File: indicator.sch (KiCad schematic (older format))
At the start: 5 parts, among them U420 2N7002DW

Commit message: added test points
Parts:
- added J? (x2): TEST_1P, SFUSat:Measurement_Point_Round-SMD-Pad_Big, symbol TEST_1P
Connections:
- wire segments 10 -> 11
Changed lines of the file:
@@
 Connection ~ 6425 3025
 Wire Wire Line
-	6125 3025 6425 3025
-Wire Wire Line
-	6425 3025 6725 3025
+	6125 3025 6725 3025
 Wire Wire Line
 	4975 3775 5075 3775
@@
 Text HLabel 6725 3025 2    54   Input ~ 0
 3V3
+$Comp
+L TEST_1P J?
+U 1 1 5AD72D99
+P 5025 3700
+AR Path="/5AC903D9/5AD72D99" Ref="J?"  Part="1"
+AR Path="/5AC9A534/5AD72D99" Ref="J?"  Part="1"
+F 0 "J?" H 5025 3970 50  0000 C CNN
+F 1 "TEST_1P" H 5025 3900 50  0000 C CNN
+F 2 "SFUSat:Measurement_Point_Round-SMD-Pad_Big" H 5225 3700 50  0001 C CNN
+F 3 "" H 5225 3700 50  0001 C CNN
+	1    5025 3700
+	1    0    0    -1
+$EndComp
+$Comp
+L TEST_1P J?
+U 1 1 5AD72E22
+P 5025 4050
+AR Path="/5AC903D9/5AD72E22" Ref="J?"  Part="1"
+AR Path="/5AC9A534/5AD72E22" Ref="J?"  Part="1"
+F 0 "J?" H 5025 4320 50  0000 C CNN
+F 1 "TEST_1P" H 5025 4250 50  0000 C CNN
+F 2 "SFUSat:Measurement_Point_Round-SMD-Pad_Big" H 5225 4050 50  0001 C CNN
+F 3 "" H 5225 4050 50  0001 C CNN
+	1    5025 4050
+	-1   0    0    1
+$EndComp
+Wire Wire Line
+	5025 3700 5025 3775
+Connection ~ 5025 3775
+Wire Wire Line
+	5025 3975 5025 4050
+Connection ~ 5025 3975
 $EndSCHEMATC

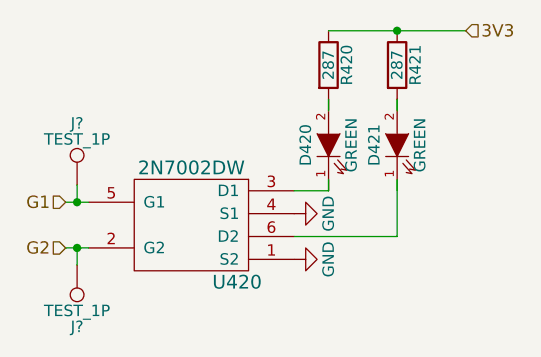
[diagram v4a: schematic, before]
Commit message: Annotated the schematics
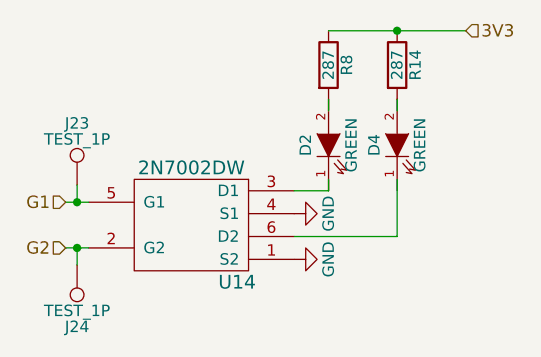
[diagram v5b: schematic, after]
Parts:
- gave numbers to parts that had none: 2
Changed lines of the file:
@@
 P 5525 3875
 AR Path="/5AC903D9/5AC92C0F" Ref="U420"  Part="1"
-AR Path="/5AC9A534/5AC92C0F" Ref="U?"  Part="1"
-F 0 "U?" H 5725 3625 60  0000 C CNN
+AR Path="/5AC9A534/5AC92C0F" Ref="U14"  Part="1"
+F 0 "U14" H 5725 3625 60  0000 C CNN
 F 1 "2N7002DW" H 5525 4125 60  0000 C CNN
 F 2 "SFUSat:SOT-363" H 5525 3875 60  0001 C CNN
@@
 P 6125 3525
 AR Path="/5AC903D9/5AC92C16" Ref="D420"  Part="1"
-AR Path="/5AC9A534/5AC92C16" Ref="D?"  Part="1"
-F 0 "D?" H 6125 3625 50  0000 C CNN
+AR Path="/5AC9A534/5AC92C16" Ref="D2"  Part="1"
+F 0 "D2" H 6125 3625 50  0000 C CNN
 F 1 "GREEN" H 6125 3425 50  0000 C CNN
 F 2 "SFUSat:LED_0603" H 6125 3525 50  0001 C CNN
@@
 P 6125 3175
 AR Path="/5AC903D9/5AC92C1D" Ref="R420"  Part="1"
-AR Path="/5AC9A534/5AC92C1D" Ref="R?"  Part="1"
-F 0 "R?" V 6205 3175 50  0000 C CNN
+AR Path="/5AC9A534/5AC92C1D" Ref="R8"  Part="1"
+F 0 "R8" V 6205 3175 50  0000 C CNN
 F 1 "287" V 6125 3175 50  0000 C CNN
 F 2 "SFUSat:R_0402" V 6055 3175 50  0001 C CNN
@@
 P 6425 3175
 AR Path="/5AC903D9/5AC92C24" Ref="R421"  Part="1"
-AR Path="/5AC9A534/5AC92C24" Ref="R?"  Part="1"
-F 0 "R?" V 6505 3175 50  0000 C CNN
+AR Path="/5AC9A534/5AC92C24" Ref="R14"  Part="1"
+F 0 "R14" V 6505 3175 50  0000 C CNN
 F 1 "287" V 6425 3175 50  0000 C CNN
 F 2 "SFUSat:R_0402" V 6355 3175 50  0001 C CNN
@@
 P 6425 3525
 AR Path="/5AC903D9/5AC92C2B" Ref="D421"  Part="1"
-AR Path="/5AC9A534/5AC92C2B" Ref="D?"  Part="1"
-F 0 "D?" H 6425 3625 50  0000 C CNN
+AR Path="/5AC9A534/5AC92C2B" Ref="D4"  Part="1"
+F 0 "D4" H 6425 3625 50  0000 C CNN
 F 1 "GREEN" H 6425 3425 50  0000 C CNN
 F 2 "SFUSat:LED_0603" H 6425 3525 50  0001 C CNN
@@
 $EndComp
 $Comp
-L GND #PWR?
+L GND #PWR105
 U 1 1 5AC92C32
 P 5975 3825
-AR Path="/5AC903D9/5AC92C32" Ref="#PWR?"  Part="1"
-AR Path="/5AC9A534/5AC92C32" Ref="#PWR?"  Part="1"
-F 0 "#PWR?" H 5975 3575 50  0001 C CNN
+AR Path="/5AC903D9/5AC92C32" Ref="#PWR105"  Part="1"
+AR Path="/5AC9A534/5AC92C32" Ref="#PWR107"  Part="1"
+F 0 "#PWR107" H 5975 3575 50  0001 C CNN
 F 1 "GND" H 5975 3675 50  0000 C CNN
 F 2 "" H 5975 3825 50  0000 C CNN
@@
 $EndComp
 $Comp
-L GND #PWR?
+L GND #PWR106
 U 1 1 5AC92C38
 P 5975 4025
-AR Path="/5AC903D9/5AC92C38" Ref="#PWR?"  Part="1"
-AR Path="/5AC9A534/5AC92C38" Ref="#PWR?"  Part="1"
-F 0 "#PWR?" H 5975 3775 50  0001 C CNN
+AR Path="/5AC903D9/5AC92C38" Ref="#PWR106"  Part="1"
+AR Path="/5AC9A534/5AC92C38" Ref="#PWR108"  Part="1"
+F 0 "#PWR108" H 5975 3775 50  0001 C CNN
 F 1 "GND" H 5975 3875 50  0000 C CNN
 F 2 "" H 5975 4025 50  0000 C CNN
@@
 3V3
 $Comp
-L TEST_1P J?
+L TEST_1P J21
 U 1 1 5AD72D99
 P 5025 3700
-AR Path="/5AC903D9/5AD72D99" Ref="J?"  Part="1"
-AR Path="/5AC9A534/5AD72D99" Ref="J?"  Part="1"
-F 0 "J?" H 5025 3970 50  0000 C CNN
+AR Path="/5AC903D9/5AD72D99" Ref="J21"  Part="1"
+AR Path="/5AC9A534/5AD72D99" Ref="J23"  Part="1"
+F 0 "J23" H 5025 3970 50  0000 C CNN
 F 1 "TEST_1P" H 5025 3900 50  0000 C CNN
 F 2 "SFUSat:Measurement_Point_Round-SMD-Pad_Big" H 5225 3700 50  0001 C CNN
@@
 $EndComp
 $Comp
-L TEST_1P J?
+L TEST_1P J22
 U 1 1 5AD72E22
 P 5025 4050
-AR Path="/5AC903D9/5AD72E22" Ref="J?"  Part="1"
-AR Path="/5AC9A534/5AD72E22" Ref="J?"  Part="1"
-F 0 "J?" H 5025 4320 50  0000 C CNN
+AR Path="/5AC903D9/5AD72E22" Ref="J22"  Part="1"
+AR Path="/5AC9A534/5AD72E22" Ref="J24"  Part="1"
+F 0 "J24" H 5025 4320 50  0000 C CNN
 F 1 "TEST_1P" H 5025 4250 50  0000 C CNN
 F 2 "SFUSat:Measurement_Point_Round-SMD-Pad_Big" H 5225 4050 50  0001 C CNN
